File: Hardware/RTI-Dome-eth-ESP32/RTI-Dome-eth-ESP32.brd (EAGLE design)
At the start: 111.1 x 76.3 mm, 102 parts, among them IC2 24LC64T-I/SN, IC3 LM2679SD-5.0_NOPB, IC8 REG1117-3.3V, J1 691313510003, J10 691313510002, J11 691313510002, J12 691313510002, J2 XT60PW-M, J3 691313510003, J4 691313510003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

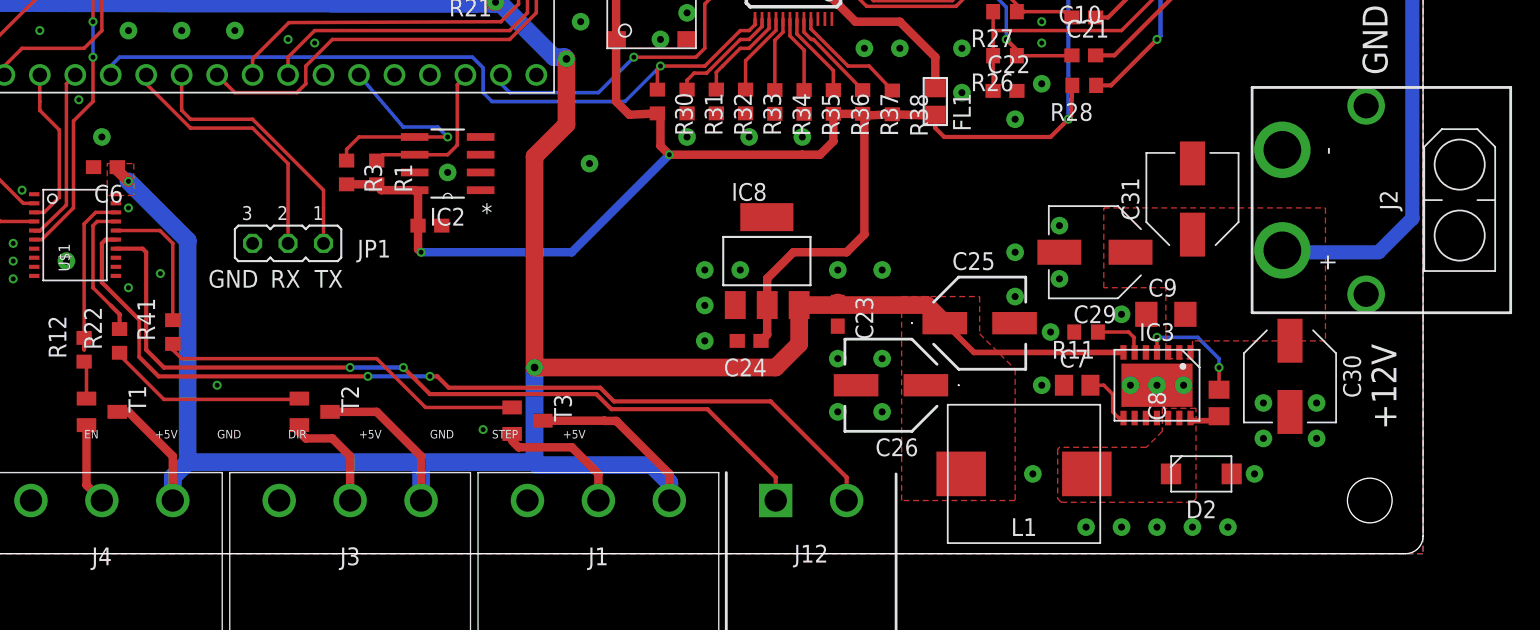
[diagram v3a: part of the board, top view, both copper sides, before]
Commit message: Change the 5V regulator on the rotatyor esp32 board.
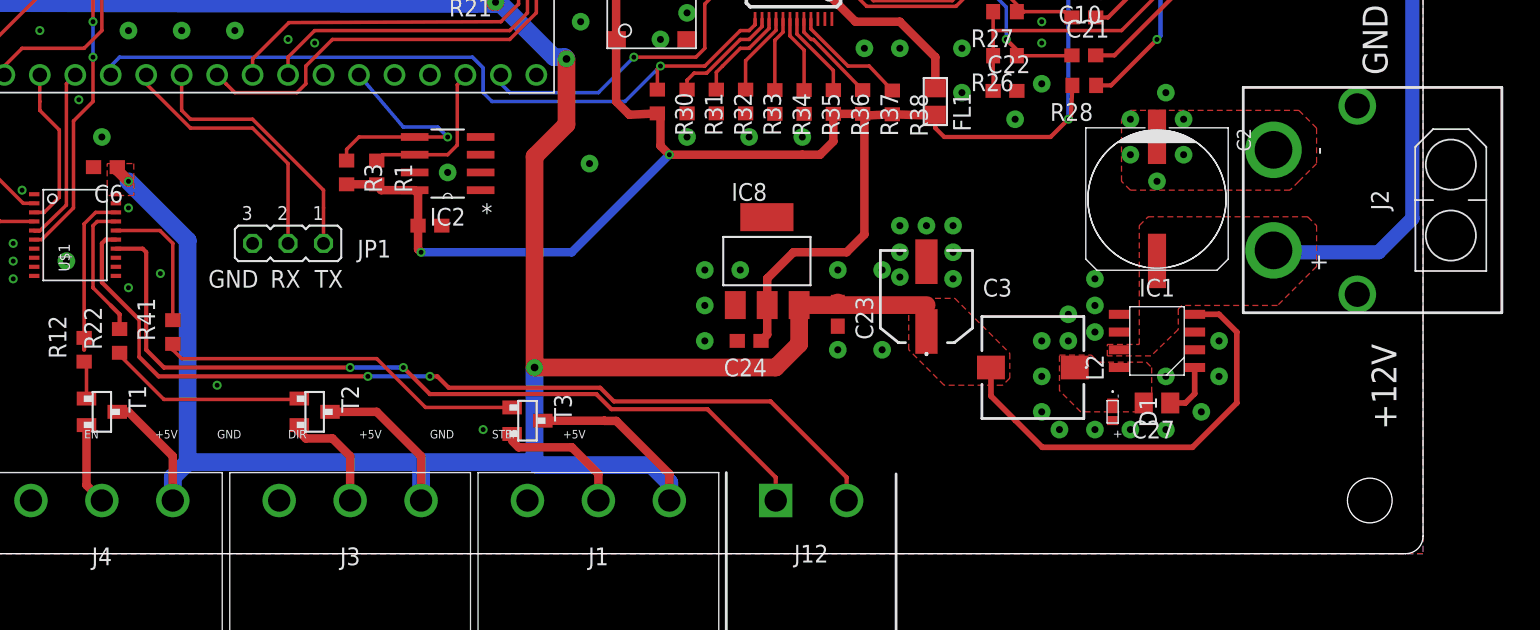
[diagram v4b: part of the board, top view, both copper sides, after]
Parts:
- removed C25, C26: 180uF, samacsys:EEE0JA331XP
- removed C29, C30, C31: 15uF 50V, samacsys:CAPAE660X550N
- removed C7: 1nF, rcl:C0805
- removed C8: 10nF, rcl:C0805
- removed C9: 470nF, rcl:C1206
- removed D2: VSSAF5L45-M3_6A, samacsys:SODFL5226X100N
- removed IC3: LM2679SD-5.0_NOPB, samacsys:SON80P500X600X100-15N
- removed L1: SRP1038CC-220M, samacsys:INDPM110100X400N
- removed R11: 5.6K, rcl:R0603
- added C2: 100uF, samacsys:UD-10X10_NICHICON
- added C27: 10nF, rcl:C0805
- added C3: 68uF, samacsys:EEEHP1H4R7P
- added D1: PMEG4015EPK,315, samacsys:PMEG4015EPK315
- added IC1: LM2675MX-5.0_NOPB, samacsys:SOIC127P600X175-8N
- added L2: 68uH, samacsys:784777470
- moved J2 0.64 mm to (100.4, 25.3)
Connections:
- removed net 5V_SW: C8.1, D2.1, IC3.12, IC3.13, IC3.14, L1.1
- removed net CB: C8.2, IC3.4
- removed net N$1: IC3.6, R11.1
- removed net N$4: C7.2, IC3.8
- new net N$2: C27.1, IC1.1
- new net SWV: C27.2, D1.1, IC1.8, L2.1
- net +12V: now also C2.+, IC1.7; no longer C29.1, C30.1, C31.1, C9.2, IC3.2, IC3.3
- net GND: now also C2.-, C3.2, D1.2, IC1.6; no longer C25.2, C26.2, C29.2, C30.2, C31.2, C7.1, C9.1, D2.2, IC3.15, IC3.9, R11.2
- net VCC: now also C3.1, IC1.4, L2.2; no longer C25.1, C26.1, IC3.7, L1.2
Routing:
- net VCC: track 258.6 -> 274.2 mm
- net CB: track 8.38 -> 0.00 mm, vias 2 -> 0
- net N$4: track 4.08 -> 0.00 mm
- net N$2: track 0.00 -> 3.90 mm
- net N$1: track 3.84 -> 0.00 mm
- net 5V_SW: track 2.26 -> 0.00 mm
- net +12V: track 129.6 -> 130.2 mm
- added copper zone on layer 1, net SWV
- removed copper zone on layer 1, net 5V_SW

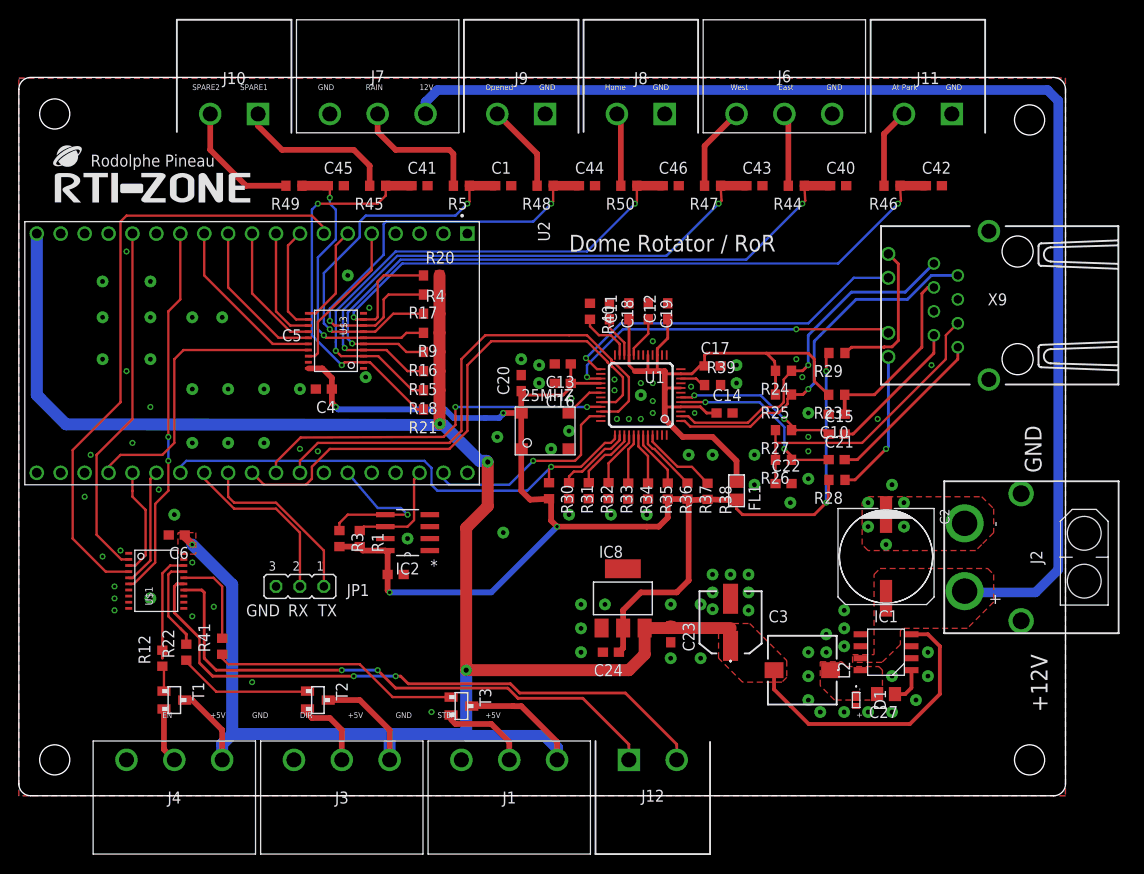
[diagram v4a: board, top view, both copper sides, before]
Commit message: Fix components orientation in the library to match JLCPCB
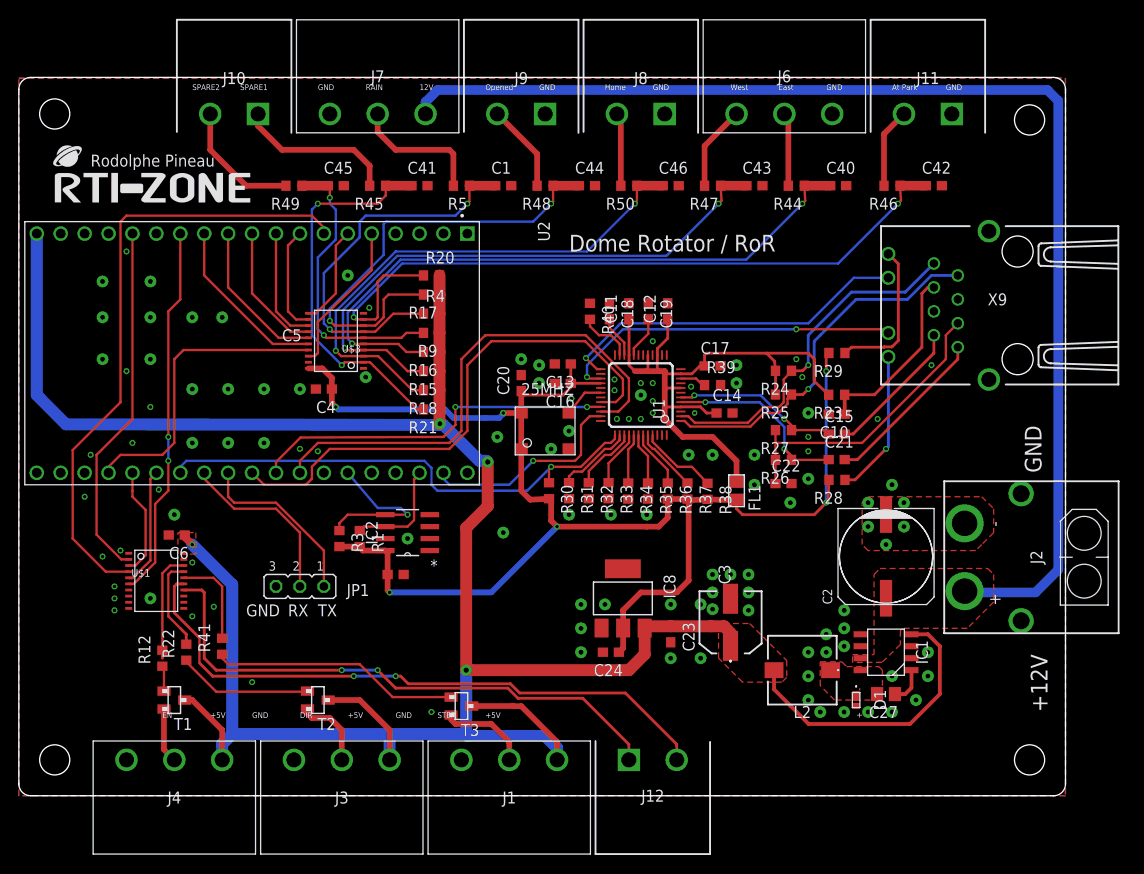
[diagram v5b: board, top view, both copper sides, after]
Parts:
- IC2: device Microchip_By_element14_Batch_1:SOIC127P600X175-8N -> rti:SOIC127P600X175-8N
- L2: value 68uH -> 47uH
- R23: value 10 1% -> 10.0 1%
- U2: value ESP32-DevKitC ESP32-WROOM-32U -> ESP32-DevKitC-32UE
- moved 25MHZ 0.63 mm to (55.9, 38.7)
- turned C2 to 90 degrees
- turned C3 to 90 degrees
- turned IC1 to 90 degrees
- turned IC2 to 90 degrees
- turned IC8 to 270 degrees
- turned L2 to 180 degrees
- turned T1 to 180 degrees
- turned T2 to 180 degrees
- turned T3 to 180 degrees
- turned U$1 to 270 degrees
- turned U$3 to 90 degrees
- turned U1 to 90 degrees
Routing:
- net VCC: track 274.2 -> 275.7 mm

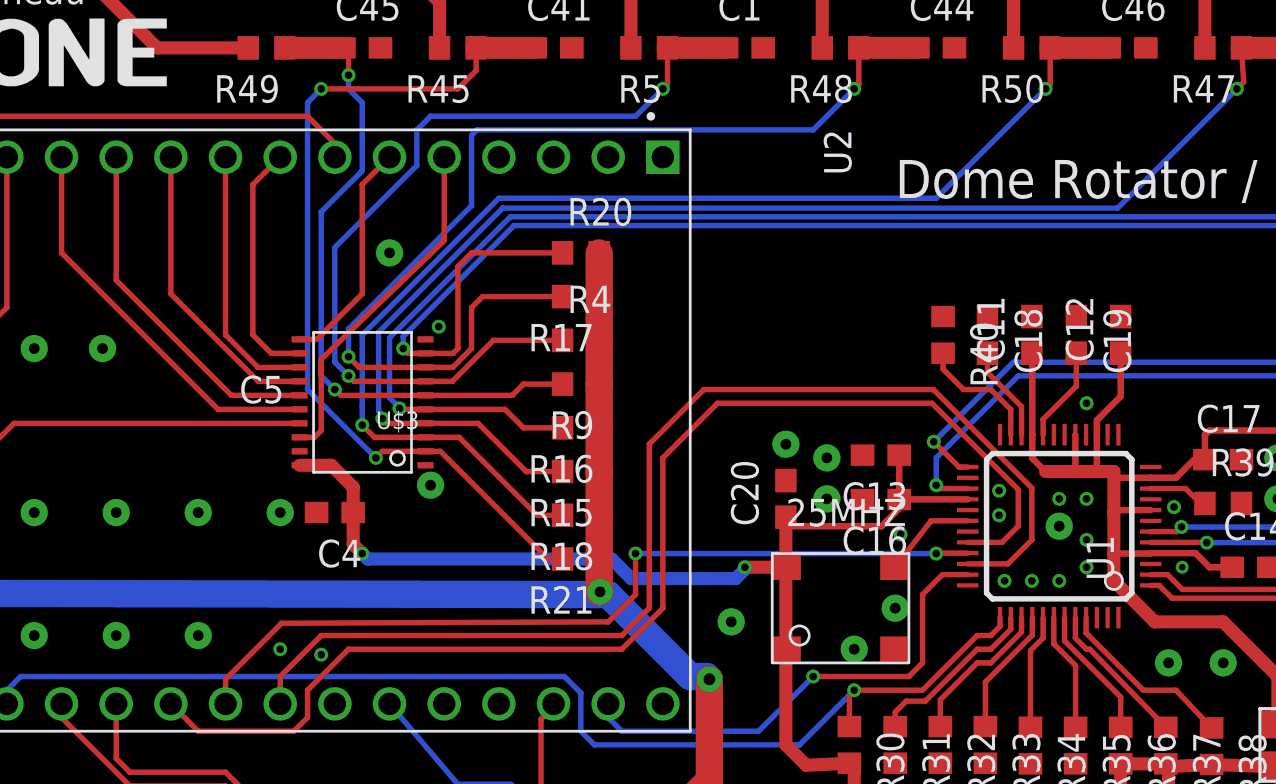
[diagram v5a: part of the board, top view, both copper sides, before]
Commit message: Re-adding the domeClient.stop();
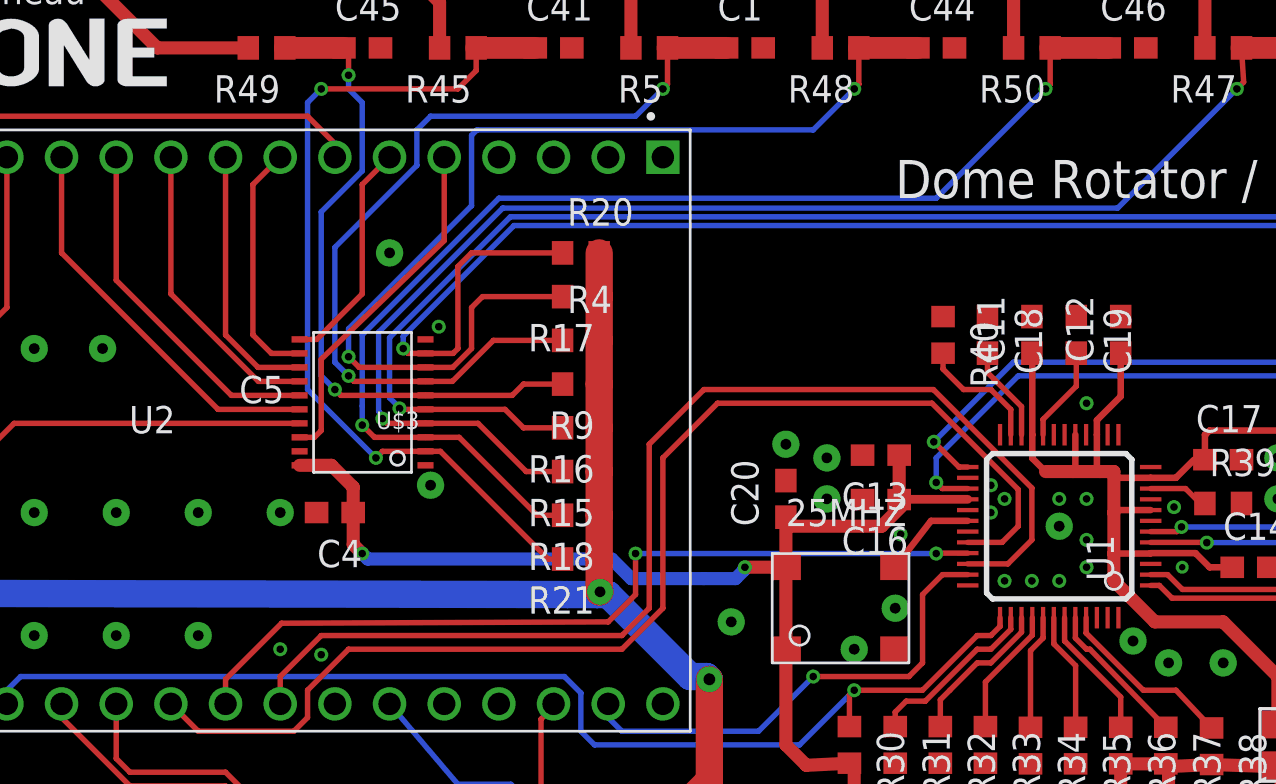
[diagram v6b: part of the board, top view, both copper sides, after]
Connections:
- net N$10 renamed L_LED+
- net N$11 renamed RD+
- net N$12 renamed RD-
- net N$13 renamed CT
- net N$7 renamed CR
- net N$8 renamed R_LED+
